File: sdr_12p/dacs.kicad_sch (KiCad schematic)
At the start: 1 part, among them U5 ADAU1962AWBSTZ

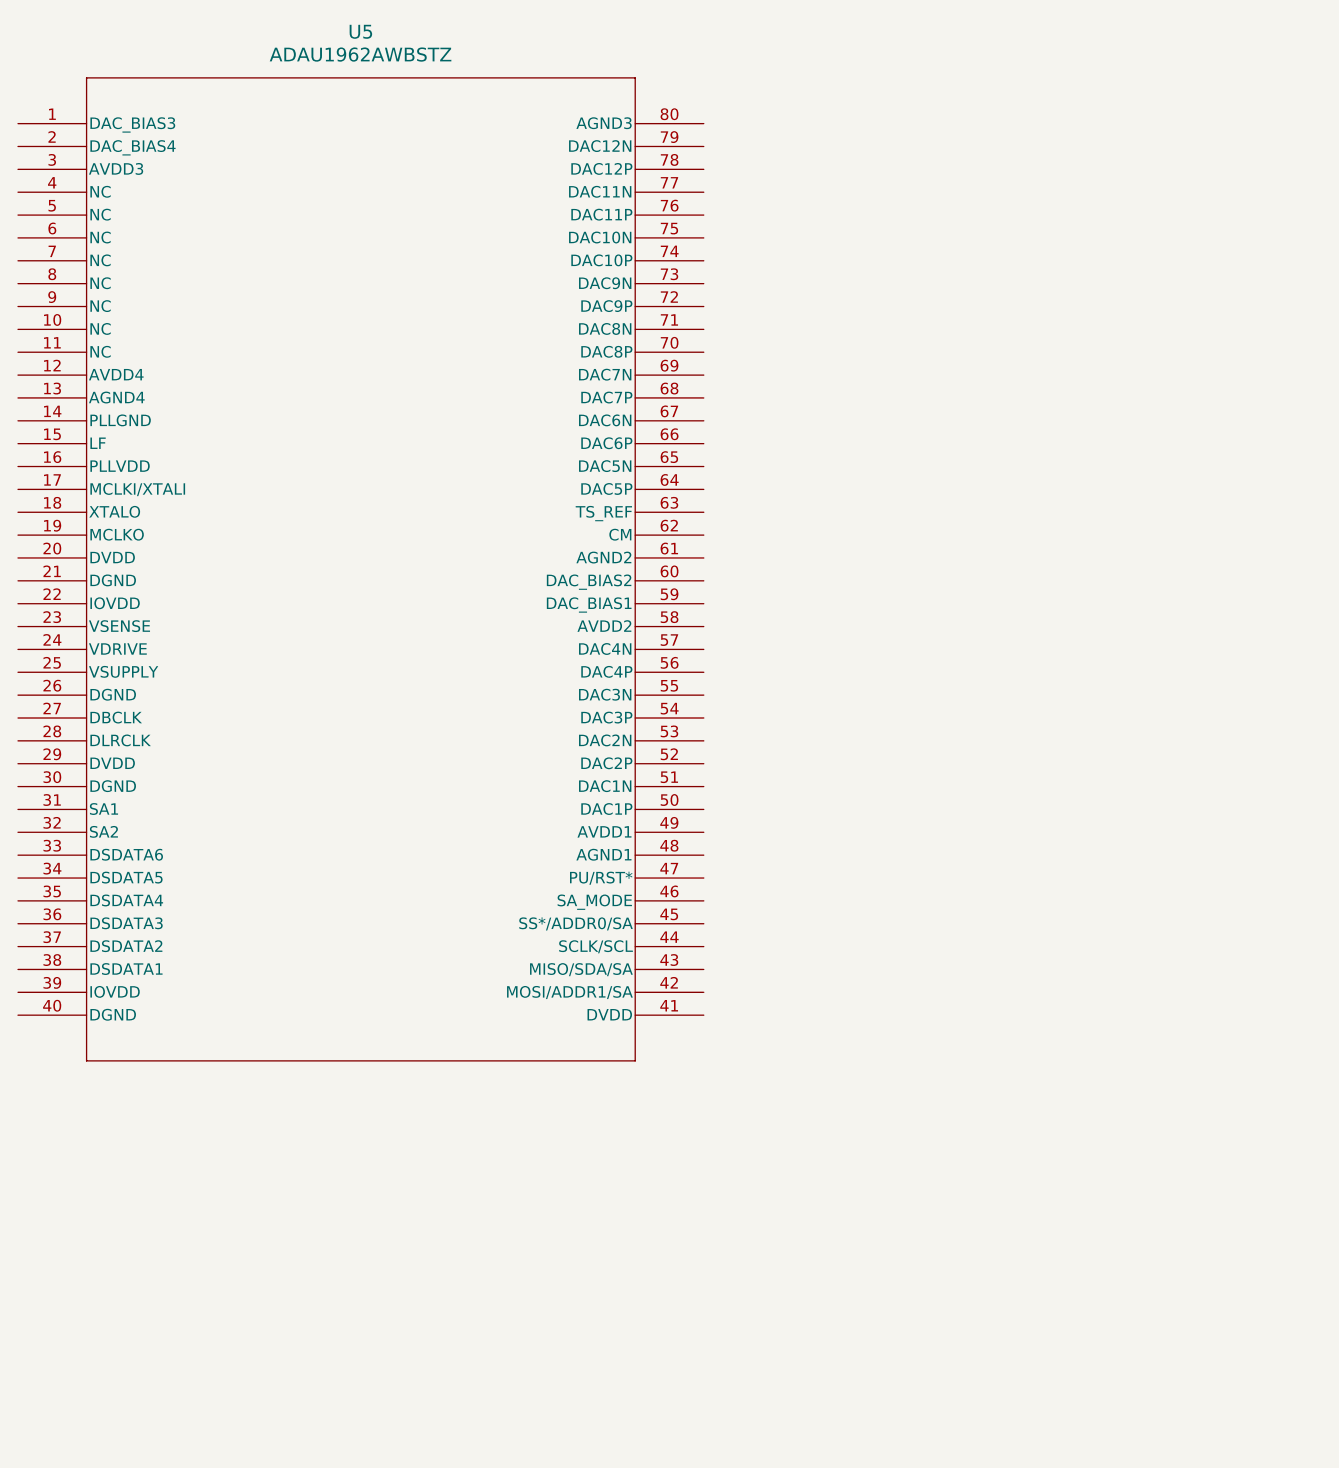
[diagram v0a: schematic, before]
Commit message: added uC
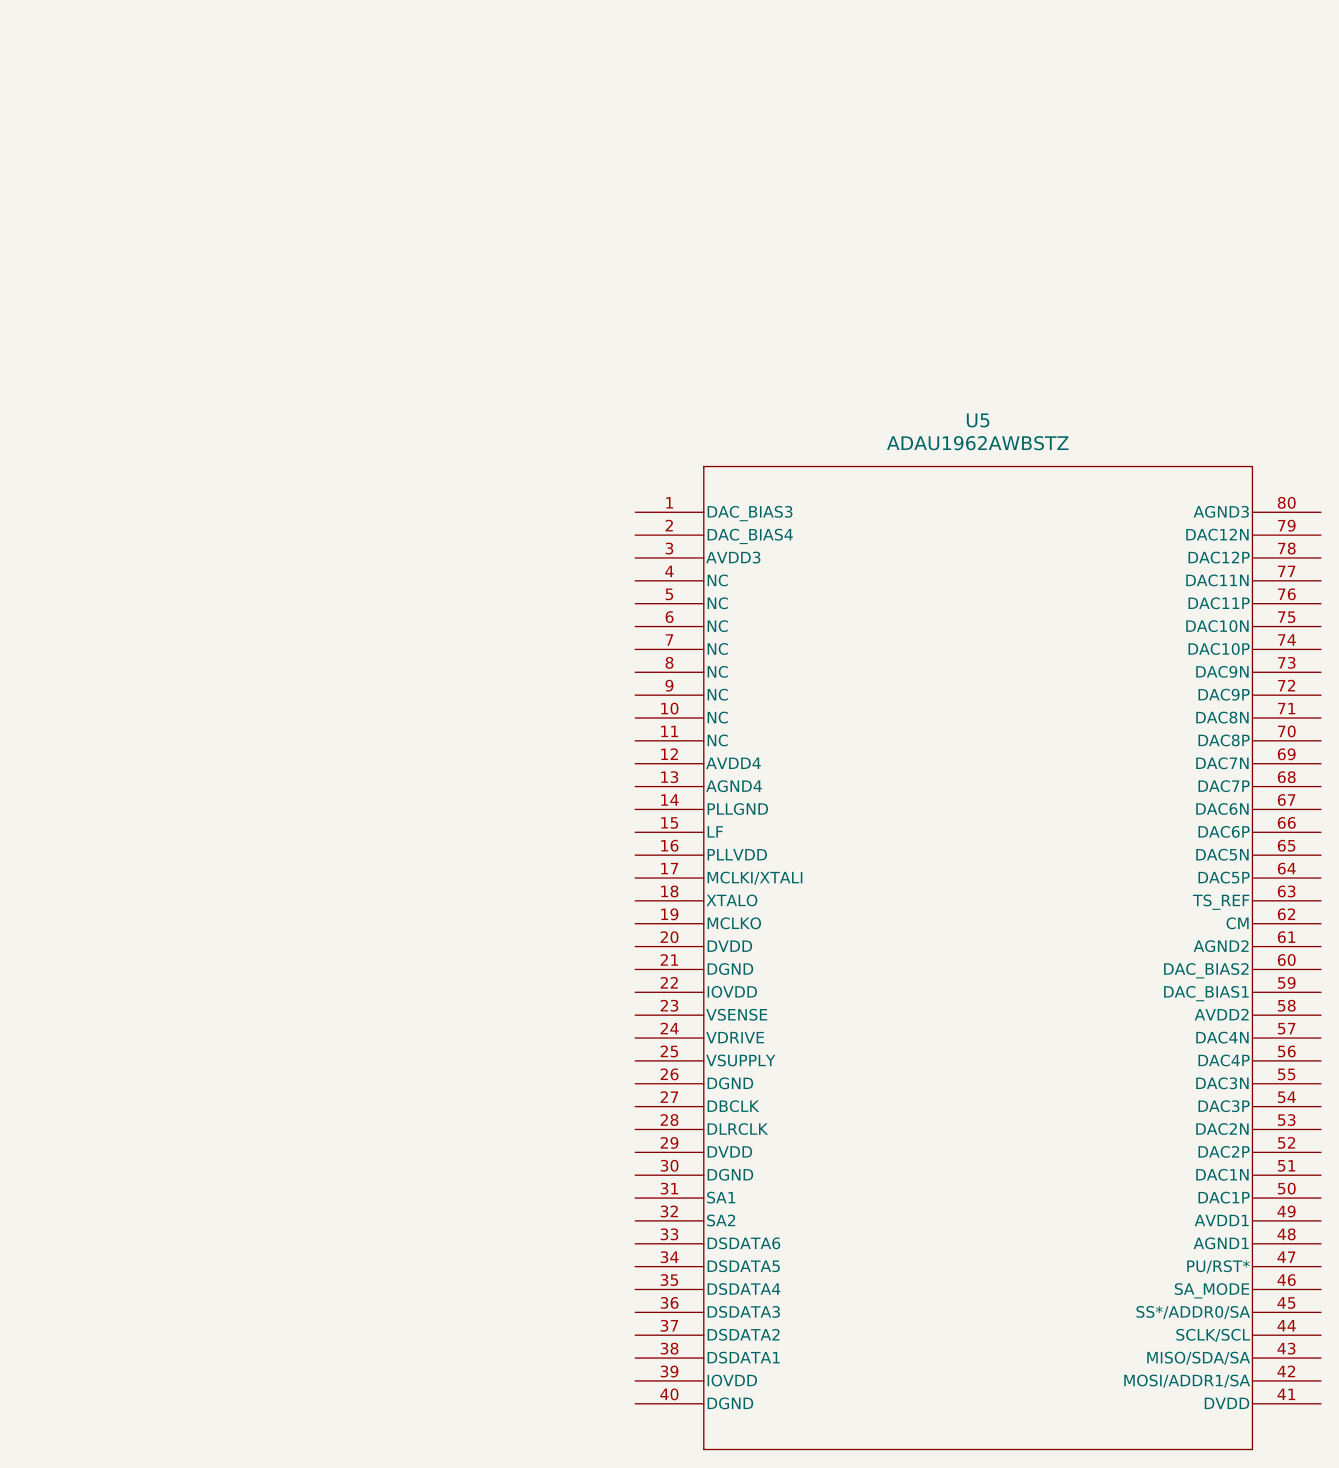
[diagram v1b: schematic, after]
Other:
- moved on the sheet: U5
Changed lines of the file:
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@@
 	(symbol
 		(lib_id "ADAU1962A:ADAU1962AWBSTZ")
-		(at 102.87 35.56 0)
+		(at 171.45 78.74 0)
 		(unit 1)
 		(exclude_from_sim no)
@@
 		(fields_autoplaced yes)
 		(property "Reference" "U5"
-			(at 140.97 25.4 0)
+			(at 209.55 68.58 0)
 			(effects
 				(font
@@
 		)
 		(property "Value" "ADAU1962AWBSTZ"
-			(at 140.97 27.94 0)
+			(at 209.55 71.12 0)
 			(effects
 				(font
@@
 		)
 		(property "Footprint" "ST_80_2_ADI"
-			(at 102.87 35.56 0)
+			(at 171.45 78.74 0)
 			(effects
 				(font
@@
 		)
 		(property "Datasheet" "https://www.analog.com/media/en/technical-documentation/data-sheets/ADAU1962A.pdf"
-			(at 102.87 35.56 0)
+			(at 171.45 78.74 0)
 			(effects
 				(font
@@
 		)
 		(property "Description" ""
-			(at 102.87 35.56 0)
+			(at 171.45 78.74 0)
 			(effects
 				(font
